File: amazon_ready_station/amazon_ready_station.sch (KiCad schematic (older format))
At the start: 29 parts, among them J7 BRKOUT_LEFT, J8 BRKOUT_RIGHT, Q1 2N2219

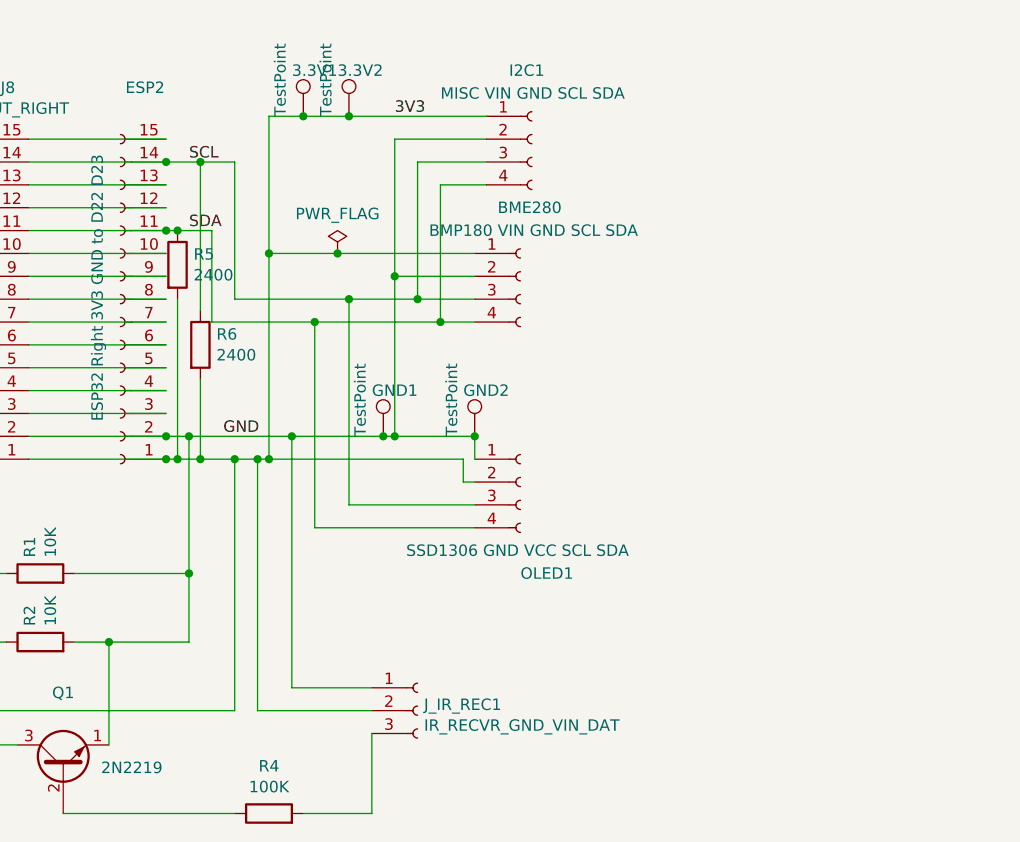
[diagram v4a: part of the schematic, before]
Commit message: pcb with receiver components
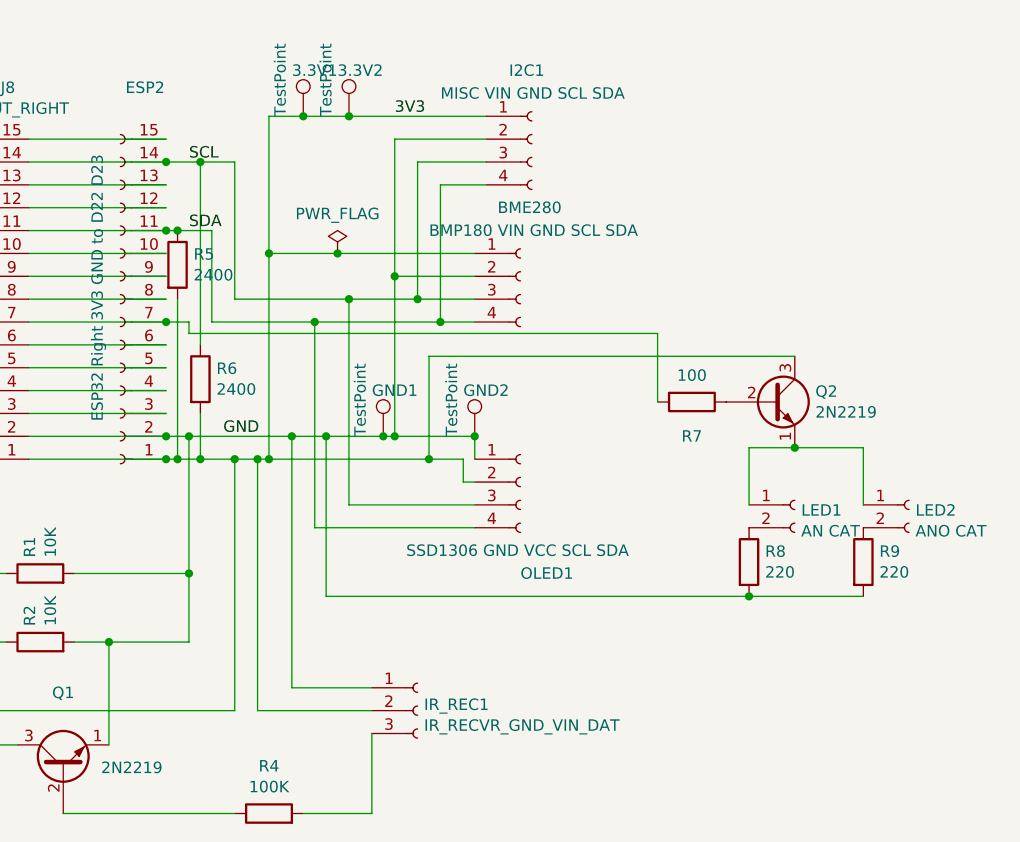
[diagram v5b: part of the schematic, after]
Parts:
- added LED1: AN CAT, Connector_PinSocket_2.54mm:PinSocket_1x02_P2.54mm_Vertical, symbol Connector:Conn_01x02_Female
- added LED2: ANO CAT, Connector_PinSocket_2.54mm:PinSocket_1x02_P2.54mm_Vertical, symbol Connector:Conn_01x02_Female
- added Q2: 2N2219, Package_TO_SOT_SMD:SOT-23_Handsoldering, symbol Transistor_BJT:2N2219
- added R7: 100, Resistor_SMD:R_0805_2012Metric_Pad1.20x1.40mm_HandSolder, symbol Device:R
- added R8, R9: 220, Resistor_SMD:R_0805_2012Metric_Pad1.20x1.40mm_HandSolder, symbol Device:R
- renumbered J_IR_REC1 to IR_REC1
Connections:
- net 3V3: now also Q2.3 (C)
- net GND: now also R8.2, R9.2
- net at ESP2.7 (Pin_7), J8.7 (Pin_7): now also R7.2
- new net: LED1.1 (Pin_1), LED2.1 (Pin_1), Q2.1 (E)
- new net: Q2.2 (B), R7.1
- new net: LED2.2 (Pin_2), R9.1
- new net: LED1.2 (Pin_2), R8.1
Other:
- moved on the sheet: R6
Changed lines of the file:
@@
 	4650 6400 3900 6400
 $Comp
-L Connector:Conn_01x03_Female J_IR_REC1
+L Connector:Conn_01x03_Female IR_REC1
 U 1 1 60683231
 P 5450 5950
-F 0 "J_IR_REC1" H 5478 5976 50  0000 L CNN
+F 0 "IR_REC1" H 5478 5976 50  0000 L CNN
 F 1 "IR_RECVR_GND_VIN_DAT" H 5478 5885 50  0000 L CNN
 F 2 "Connector_PinSocket_2.54mm:PinSocket_1x03_P2.54mm_Horizontal" H 5450 5950 50  0001 C CNN
@@
 Connection ~ 5350 4750
 Wire Wire Line
-	4800 4850 5650 4850
+	4800 4850 5500 4850
 Wire Wire Line
 	5650 4850 5650 4950
@@
 Connection ~ 4900 4750
 Wire Wire Line
-	4900 4750 5300 4750
+	4900 4750 5050 4750
 Wire Wire Line
 	4750 4850 4750 5950
@@
 L Device:R R6
 U 1 1 605D9489
-P 4500 4350
-F 0 "R6" H 4570 4396 50  0000 L CNN
-F 1 "2400" H 4570 4305 50  0000 L CNN
-F 2 "Resistor_SMD:R_0805_2012Metric_Pad1.20x1.40mm_HandSolder" V 4430 4350 50  0001 C CNN
-F 3 "~" H 4500 4350 50  0001 C CNN
-	1    4500 4350
-	1    0    0    -1
-$EndComp
-Wire Wire Line
-	4500 3550 4500 4200
+P 4500 4500
+F 0 "R6" H 4570 4546 50  0000 L CNN
+F 1 "2400" H 4570 4455 50  0000 L CNN
+F 2 "Resistor_SMD:R_0805_2012Metric_Pad1.20x1.40mm_HandSolder" V 4430 4500 50  0001 C CNN
+F 3 "~" H 4500 4500 50  0001 C CNN
+	1    4500 4500
+	1    0    0    -1
+$EndComp
+Wire Wire Line
+	4500 3550 4500 4350
 Connection ~ 4500 3550
 Wire Wire Line
@@
 	4500 4850 4650 4850
 Wire Wire Line
-	4500 4500 4500 4850
+	4500 4650 4500 4850
 $Comp
 L Mechanical:MountingHole H2
@@
 Text Label 5350 3350 0    50   ~ 0
 3V3
+$Comp
+L Transistor_BJT:2N2219 Q2
+U 1 1 60640972
+P 7000 4600
+F 0 "Q2" H 7190 4646 50  0000 L CNN
+F 1 "2N2219" H 7190 4555 50  0000 L CNN
+F 2 "Package_TO_SOT_SMD:SOT-23_Handsoldering" H 7200 4525 50  0001 L CIN
+F 3 "http://www.onsemi.com/pub_link/Collateral/2N2219-D.PDF" H 7000 4600 50  0001 L CNN
+	1    7000 4600
+	1    0    0    -1
+$EndComp
+Wire Wire Line
+	5500 4850 5500 4400
+Wire Wire Line
+	5500 4400 7100 4400
+Connection ~ 5500 4850
+Wire Wire Line
+	5500 4850 5650 4850
+$Comp
+L Device:R R9
+U 1 1 6064E0C0
+P 7400 5300
+F 0 "R9" H 7470 5346 50  0000 L CNN
+F 1 "220" H 7470 5255 50  0000 L CNN
+F 2 "Resistor_SMD:R_0805_2012Metric_Pad1.20x1.40mm_HandSolder" V 7330 5300 50  0001 C CNN
+F 3 "~" H 7400 5300 50  0001 C CNN
+	1    7400 5300
+	1    0    0    -1
+$EndComp
+$Comp
+L Device:R R8
+U 1 1 6064EAB3
+P 6900 5300
+F 0 "R8" H 6970 5346 50  0000 L CNN
+F 1 "220" H 6970 5255 50  0000 L CNN
+F 2 "Resistor_SMD:R_0805_2012Metric_Pad1.20x1.40mm_HandSolder" V 6830 5300 50  0001 C CNN
+F 3 "~" H 6900 5300 50  0001 C CNN
+	1    6900 5300
+	1    0    0    -1
+$EndComp
+Wire Wire Line
+	5050 4750 5050 5450
+Wire Wire Line
+	5050 5450 6900 5450
+Connection ~ 5050 4750
+Wire Wire Line
+	5050 4750 5300 4750
+Wire Wire Line
+	6900 5450 7400 5450
+Connection ~ 6900 5450
+$Comp
+L Connector:Conn_01x02_Female LED1
+U 1 1 60659CCB
+P 7100 5050
+F 0 "LED1" H 7128 5026 50  0000 L CNN
+F 1 "AN CAT" H 7128 4935 50  0000 L CNN
+F 2 "Connector_PinSocket_2.54mm:PinSocket_1x02_P2.54mm_Vertical" H 7100 5050 50  0001 C CNN
+F 3 "~" H 7100 5050 50  0001 C CNN
+	1    7100 5050
+	1    0    0    -1
+$EndComp
+$Comp
+L Connector:Conn_01x02_Female LED2
+U 1 1 6065A556
+P 7600 5050
+F 0 "LED2" H 7628 5026 50  0000 L CNN
+F 1 "ANO CAT" H 7628 4935 50  0000 L CNN
+F 2 "Connector_PinSocket_2.54mm:PinSocket_1x02_P2.54mm_Vertical" H 7600 5050 50  0001 C CNN
+F 3 "~" H 7600 5050 50  0001 C CNN
+	1    7600 5050
+	1    0    0    -1
+$EndComp
+Wire Wire Line
+	7100 4800 6900 4800
+Wire Wire Line
+	6900 4800 6900 5050
+Wire Wire Line
+	7100 4800 7400 4800
+Wire Wire Line
+	7400 4800 7400 5050
+Connection ~ 7100 4800
+Wire Wire Line
+	4350 4250 4450 4250
+Wire Wire Line
+	4450 4250 4450 4300
+Wire Wire Line
+	4450 4300 6500 4300
+Wire Wire Line
+	6500 4300 6500 4600
+Connection ~ 4350 4250
+$Comp
+L Device:R R7
+U 1 1 60675A04
+P 6650 4600
+F 0 "R7" V 6800 4600 50  0000 C CNN
+F 1 "100" V 6534 4600 50  0000 C CNN
+F 2 "Resistor_SMD:R_0805_2012Metric_Pad1.20x1.40mm_HandSolder" V 6580 4600 50  0001 C CNN
+F 3 "~" H 6650 4600 50  0001 C CNN
+	1    6650 4600
+	0    1    1    0
+$EndComp
 $EndSCHEMATC

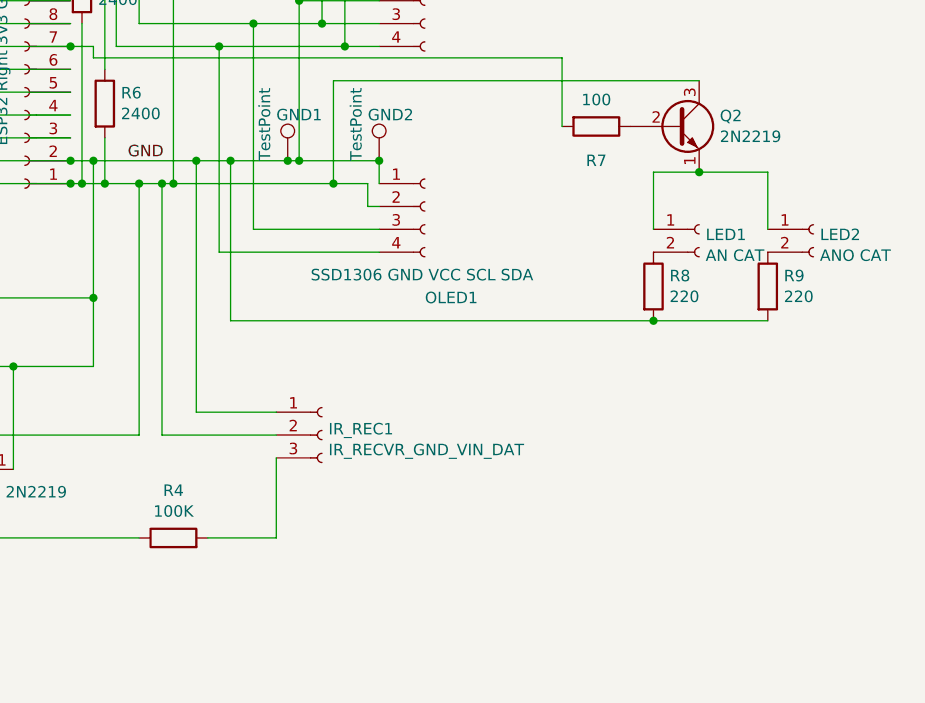
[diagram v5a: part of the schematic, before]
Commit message: moved LED to bottom, added IR Rec circuit on board
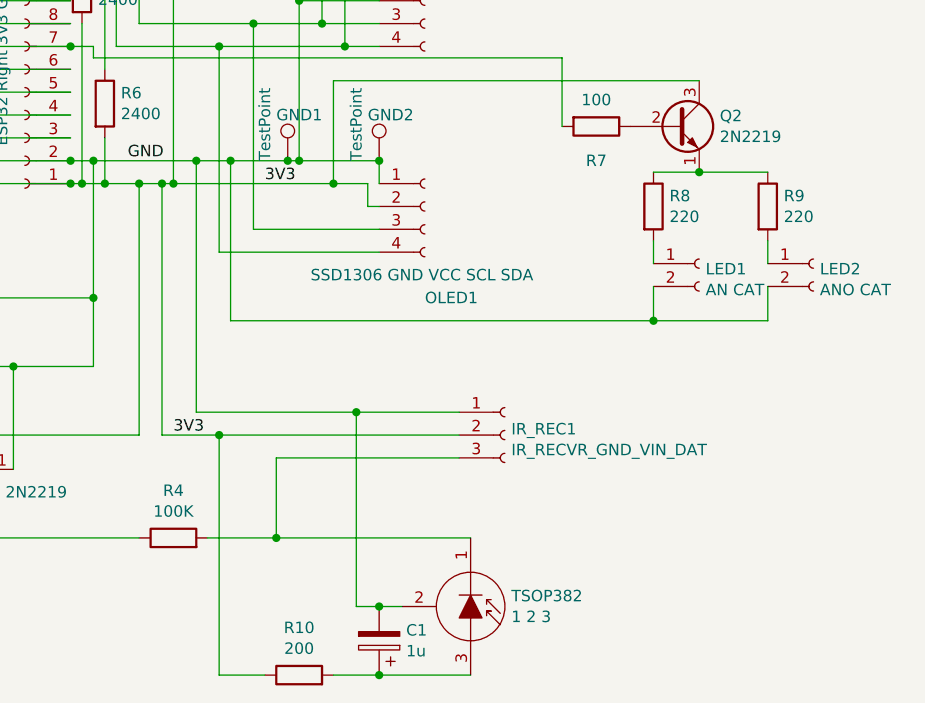
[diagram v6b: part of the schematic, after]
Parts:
- added C1: 1u, Capacitor_Tantalum_SMD:CP_EIA-1608-08_AVX-J_Pad1.25x1.05mm_HandSolder, symbol Device:CP
- added R10: 200, Resistor_SMD:R_0805_2012Metric_Pad1.20x1.40mm_HandSolder, symbol Device:R
- added TSOP382: 1 2 3, TSOP38238:XDCR_TSOP38238, symbol Sensor_Optical:S5971
- IR_REC1: footprint Connector_PinSocket_2.54mm:PinSocket_1x03_P2.54mm_Horizontal -> Connector_PinSocket_2.54mm:PinSocket_1x03_P2.54mm_Vertical
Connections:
- net 3V3: now also R10.1
- net GND: now also LED1.2 (Pin_2), LED2.2 (Pin_2), C1.2, TSOP382.2 (C); no longer R8.2, R9.2
- net at IR_REC1.3 (Pin_3), R4.2: now also TSOP382.1 (K)
- net at R9.1: now also Q2.1 (E), R8.1; no longer LED2.2 (Pin_2)
- new net: LED2.1 (Pin_1), R9.2
- new net: LED1.1 (Pin_1), R8.2
- new net: C1.1, R10.2, TSOP382.3 (A)
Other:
- moved on the sheet: IR_REC1, LED1, LED2, R8, R9
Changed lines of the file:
@@
 L Connector:Conn_01x03_Female IR_REC1
 U 1 1 60683231
-P 5450 5950
-F 0 "IR_REC1" H 5478 5976 50  0000 L CNN
-F 1 "IR_RECVR_GND_VIN_DAT" H 5478 5885 50  0000 L CNN
-F 2 "Connector_PinSocket_2.54mm:PinSocket_1x03_P2.54mm_Horizontal" H 5450 5950 50  0001 C CNN
-F 3 "~" H 5450 5950 50  0001 C CNN
-	1    5450 5950
+P 6250 5950
+F 0 "IR_REC1" H 6278 5976 50  0000 L CNN
+F 1 "IR_RECVR_GND_VIN_DAT" H 6278 5885 50  0000 L CNN
+F 2 "Connector_PinSocket_2.54mm:PinSocket_1x03_P2.54mm_Vertical" H 6250 5950 50  0001 C CNN
+F 3 "~" H 6250 5950 50  0001 C CNN
+	1    6250 5950
 	1    0    0    -1
 $EndComp
@@
 	4900 4750 4900 5850
 Wire Wire Line
-	4900 5850 5250 5850
+	4900 5850 5600 5850
 Connection ~ 4900 4750
 Wire Wire Line
@@
 	4750 4850 4750 5950
 Wire Wire Line
-	4750 5950 5250 5950
+	4750 5950 5000 5950
 Connection ~ 4750 4850
 Wire Wire Line
 	4750 4850 4800 4850
-Wire Wire Line
-	5250 6050 5250 6400
 Wire Wire Line
 	4950 6400 5250 6400
@@
 L Device:R R9
 U 1 1 6064E0C0
-P 7400 5300
-F 0 "R9" H 7470 5346 50  0000 L CNN
-F 1 "220" H 7470 5255 50  0000 L CNN
-F 2 "Resistor_SMD:R_0805_2012Metric_Pad1.20x1.40mm_HandSolder" V 7330 5300 50  0001 C CNN
-F 3 "~" H 7400 5300 50  0001 C CNN
-	1    7400 5300
+P 7400 4950
+F 0 "R9" H 7470 4996 50  0000 L CNN
+F 1 "220" H 7470 4905 50  0000 L CNN
+F 2 "Resistor_SMD:R_0805_2012Metric_Pad1.20x1.40mm_HandSolder" V 7330 4950 50  0001 C CNN
+F 3 "~" H 7400 4950 50  0001 C CNN
+	1    7400 4950
 	1    0    0    -1
 $EndComp
@@
 L Device:R R8
 U 1 1 6064EAB3
-P 6900 5300
-F 0 "R8" H 6970 5346 50  0000 L CNN
-F 1 "220" H 6970 5255 50  0000 L CNN
-F 2 "Resistor_SMD:R_0805_2012Metric_Pad1.20x1.40mm_HandSolder" V 6830 5300 50  0001 C CNN
-F 3 "~" H 6900 5300 50  0001 C CNN
-	1    6900 5300
+P 6900 4950
+F 0 "R8" H 6970 4996 50  0000 L CNN
+F 1 "220" H 6970 4905 50  0000 L CNN
+F 2 "Resistor_SMD:R_0805_2012Metric_Pad1.20x1.40mm_HandSolder" V 6830 4950 50  0001 C CNN
+F 3 "~" H 6900 4950 50  0001 C CNN
+	1    6900 4950
 	1    0    0    -1
 $EndComp
 Wire Wire Line
 	5050 4750 5050 5450
-Wire Wire Line
-	5050 5450 6900 5450
 Connection ~ 5050 4750
 Wire Wire Line
 	5050 4750 5300 4750
-Wire Wire Line
-	6900 5450 7400 5450
-Connection ~ 6900 5450
 $Comp
 L Connector:Conn_01x02_Female LED1
 U 1 1 60659CCB
-P 7100 5050
-F 0 "LED1" H 7128 5026 50  0000 L CNN
-F 1 "AN CAT" H 7128 4935 50  0000 L CNN
-F 2 "Connector_PinSocket_2.54mm:PinSocket_1x02_P2.54mm_Vertical" H 7100 5050 50  0001 C CNN
-F 3 "~" H 7100 5050 50  0001 C CNN
-	1    7100 5050
+P 7100 5200
+F 0 "LED1" H 7128 5176 50  0000 L CNN
+F 1 "AN CAT" H 7128 5085 50  0000 L CNN
+F 2 "Connector_PinSocket_2.54mm:PinSocket_1x02_P2.54mm_Vertical" H 7100 5200 50  0001 C CNN
+F 3 "~" H 7100 5200 50  0001 C CNN
+	1    7100 5200
 	1    0    0    -1
 $EndComp
@@
 L Connector:Conn_01x02_Female LED2
 U 1 1 6065A556
-P 7600 5050
-F 0 "LED2" H 7628 5026 50  0000 L CNN
-F 1 "ANO CAT" H 7628 4935 50  0000 L CNN
-F 2 "Connector_PinSocket_2.54mm:PinSocket_1x02_P2.54mm_Vertical" H 7600 5050 50  0001 C CNN
-F 3 "~" H 7600 5050 50  0001 C CNN
-	1    7600 5050
+P 7600 5200
+F 0 "LED2" H 7628 5176 50  0000 L CNN
+F 1 "ANO CAT" H 7628 5085 50  0000 L CNN
+F 2 "Connector_PinSocket_2.54mm:PinSocket_1x02_P2.54mm_Vertical" H 7600 5200 50  0001 C CNN
+F 3 "~" H 7600 5200 50  0001 C CNN
+	1    7600 5200
 	1    0    0    -1
 $EndComp
@@
 	7100 4800 6900 4800
 Wire Wire Line
-	6900 4800 6900 5050
-Wire Wire Line
 	7100 4800 7400 4800
-Wire Wire Line
-	7400 4800 7400 5050
 Connection ~ 7100 4800
 Wire Wire Line
@@
 	0    1    1    0
 $EndComp
+$Comp
+L Sensor_Optical:S5971 TSOP382
+U 1 1 60653390
+P 6100 6700
+F 0 "TSOP382" V 6054 6878 50  0000 L CNN
+F 1 "1 2 3" V 6145 6878 50  0000 L CNN
+F 2 "TSOP38238:XDCR_TSOP38238" H 6100 7050 50  0001 C CNN
+F 3 "https://www.hamamatsu.com/resources/pdf/ssd/s5971_etc_kpin1025e.pdf" H 6100 6700 50  0001 C CNN
+	1    6100 6700
+	0    1    1    0
+$EndComp
+Wire Wire Line
+	6050 6050 5250 6050
+Wire Wire Line
+	5250 6050 5250 6400
+Wire Wire Line
+	6100 6400 5250 6400
+Connection ~ 5250 6400
+Wire Wire Line
+	5600 5850 5600 6700
+Connection ~ 5600 5850
+Wire Wire Line
+	5600 5850 6050 5850
+$Comp
+L Device:R R10
+U 1 1 6068EEF5
+P 5350 7000
+F 0 "R10" V 5557 7000 50  0000 C CNN
+F 1 "200" V 5466 7000 50  0000 C CNN
+F 2 "Resistor_SMD:R_0805_2012Metric_Pad1.20x1.40mm_HandSolder" V 5280 7000 50  0001 C CNN
+F 3 "~" H 5350 7000 50  0001 C CNN
+	1    5350 7000
+	0    -1   -1   0
+$EndComp
+Wire Wire Line
+	5200 7000 5000 7000
+Wire Wire Line
+	5000 7000 5000 5950
+Connection ~ 5000 5950
+Wire Wire Line
+	5000 5950 6050 5950
+Text Label 4800 5950 0    50   ~ 0
+3V3
+Text Label 5200 4850 0    50   ~ 0
+3V3
+Wire Wire Line
+	5600 6700 5700 6700
+Wire Wire Line
+	5500 7000 5700 7000
+$Comp
+L Device:CP C1
+U 1 1 606B0062
+P 5700 6850
+F 0 "C1" H 5582 6804 50  0000 R CNN
+F 1 "1u" H 5582 6895 50  0000 R CNN
+F 2 "Capacitor_Tantalum_SMD:CP_EIA-1608-08_AVX-J_Pad1.25x1.05mm_HandSolder" H 5738 6700 50  0001 C CNN
+F 3 "~" H 5700 6850 50  0001 C CNN
+	1    5700 6850
+	-1   0    0    1
+$EndComp
+Connection ~ 5700 7000
+Wire Wire Line
+	5700 7000 6100 7000
+Connection ~ 5700 6700
+Wire Wire Line
+	5700 6700 5800 6700
+Wire Wire Line
+	5050 5450 6900 5450
+Wire Wire Line
+	6900 5100 6900 5200
+Wire Wire Line
+	6900 5300 6900 5450
+Connection ~ 6900 5450
+Wire Wire Line
+	6900 5450 7400 5450
+Wire Wire Line
+	7400 5300 7400 5450
+Wire Wire Line
+	7400 5100 7400 5200
 $EndSCHEMATC
